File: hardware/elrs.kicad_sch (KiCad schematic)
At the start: 38 parts, among them J10 5V, J11 5V, J12 5V, J26 5V, J31 5V, U12 WL9005D4-33, U19 XL-1010RGBC-WS2812B, U2 ESP32-C3FH4, U20 SX1281IMLTRT, X2 SX0B40.000F0810F30

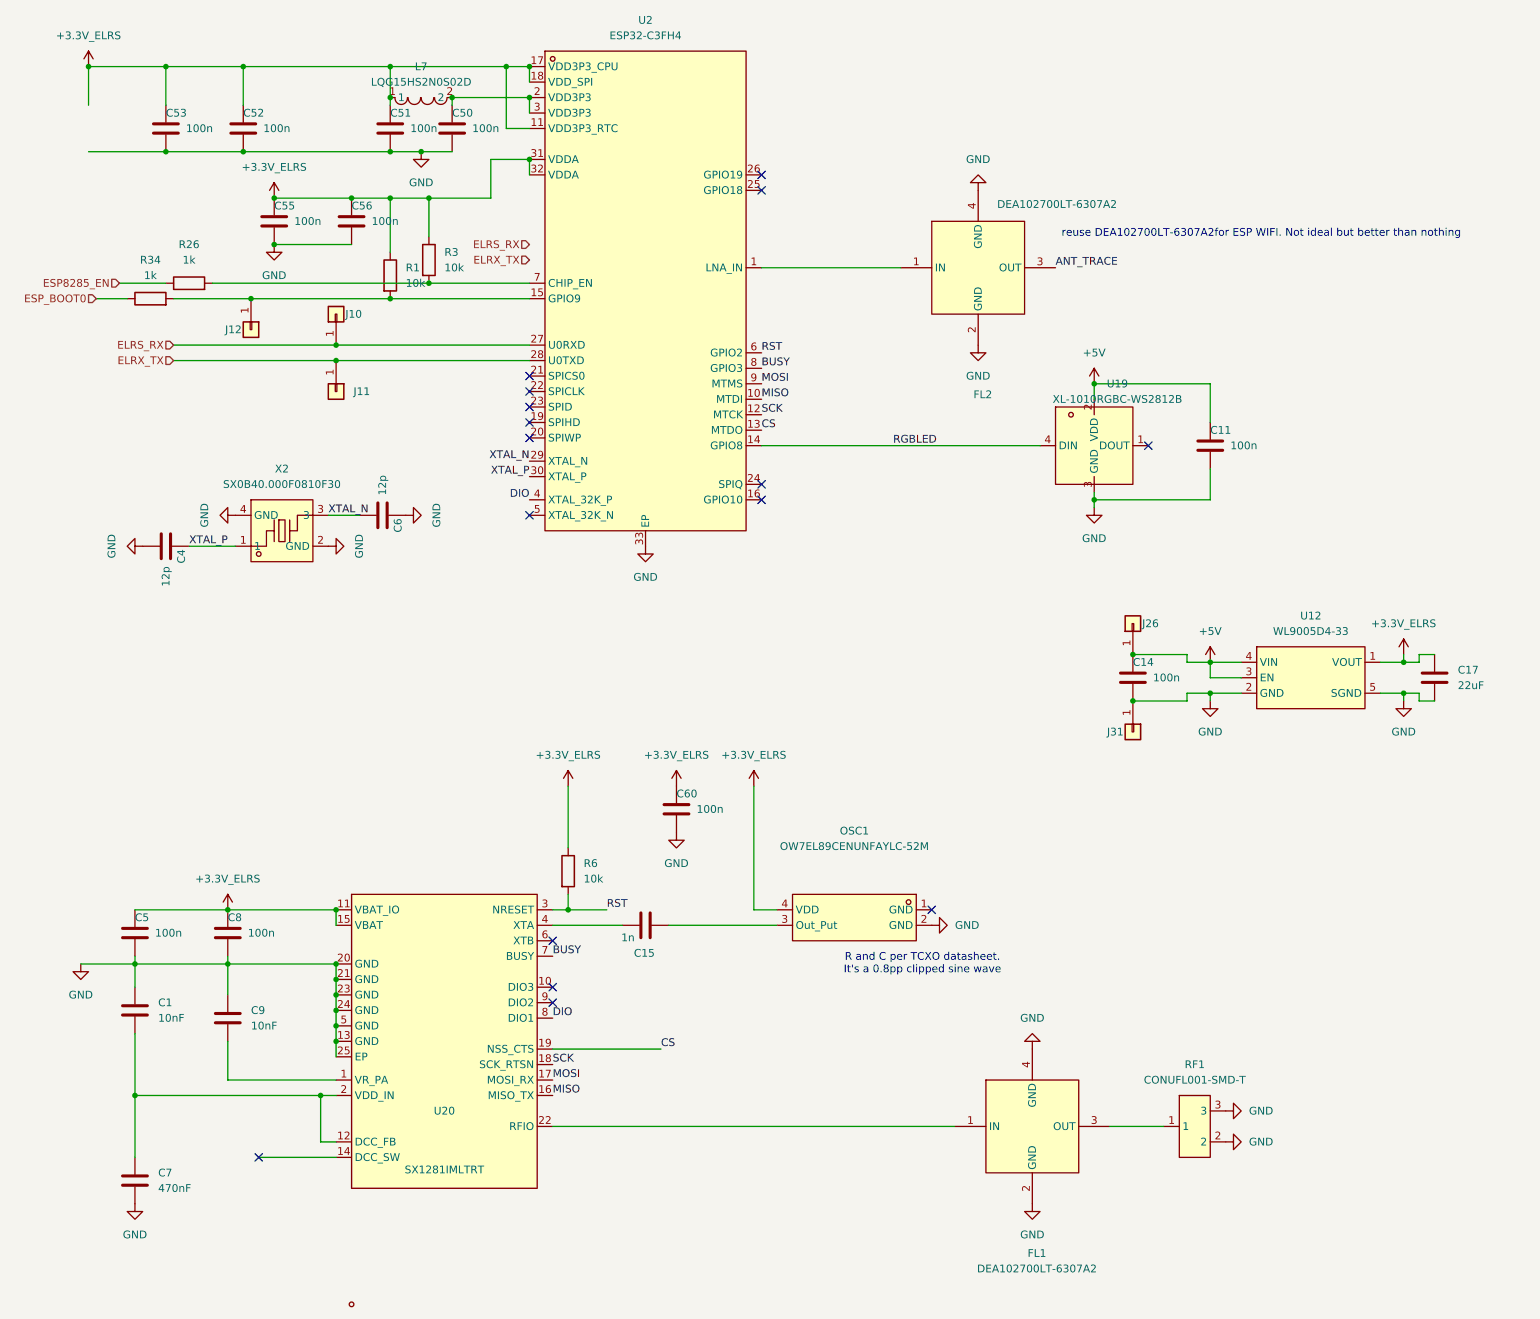
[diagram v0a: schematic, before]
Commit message: switched to 0201
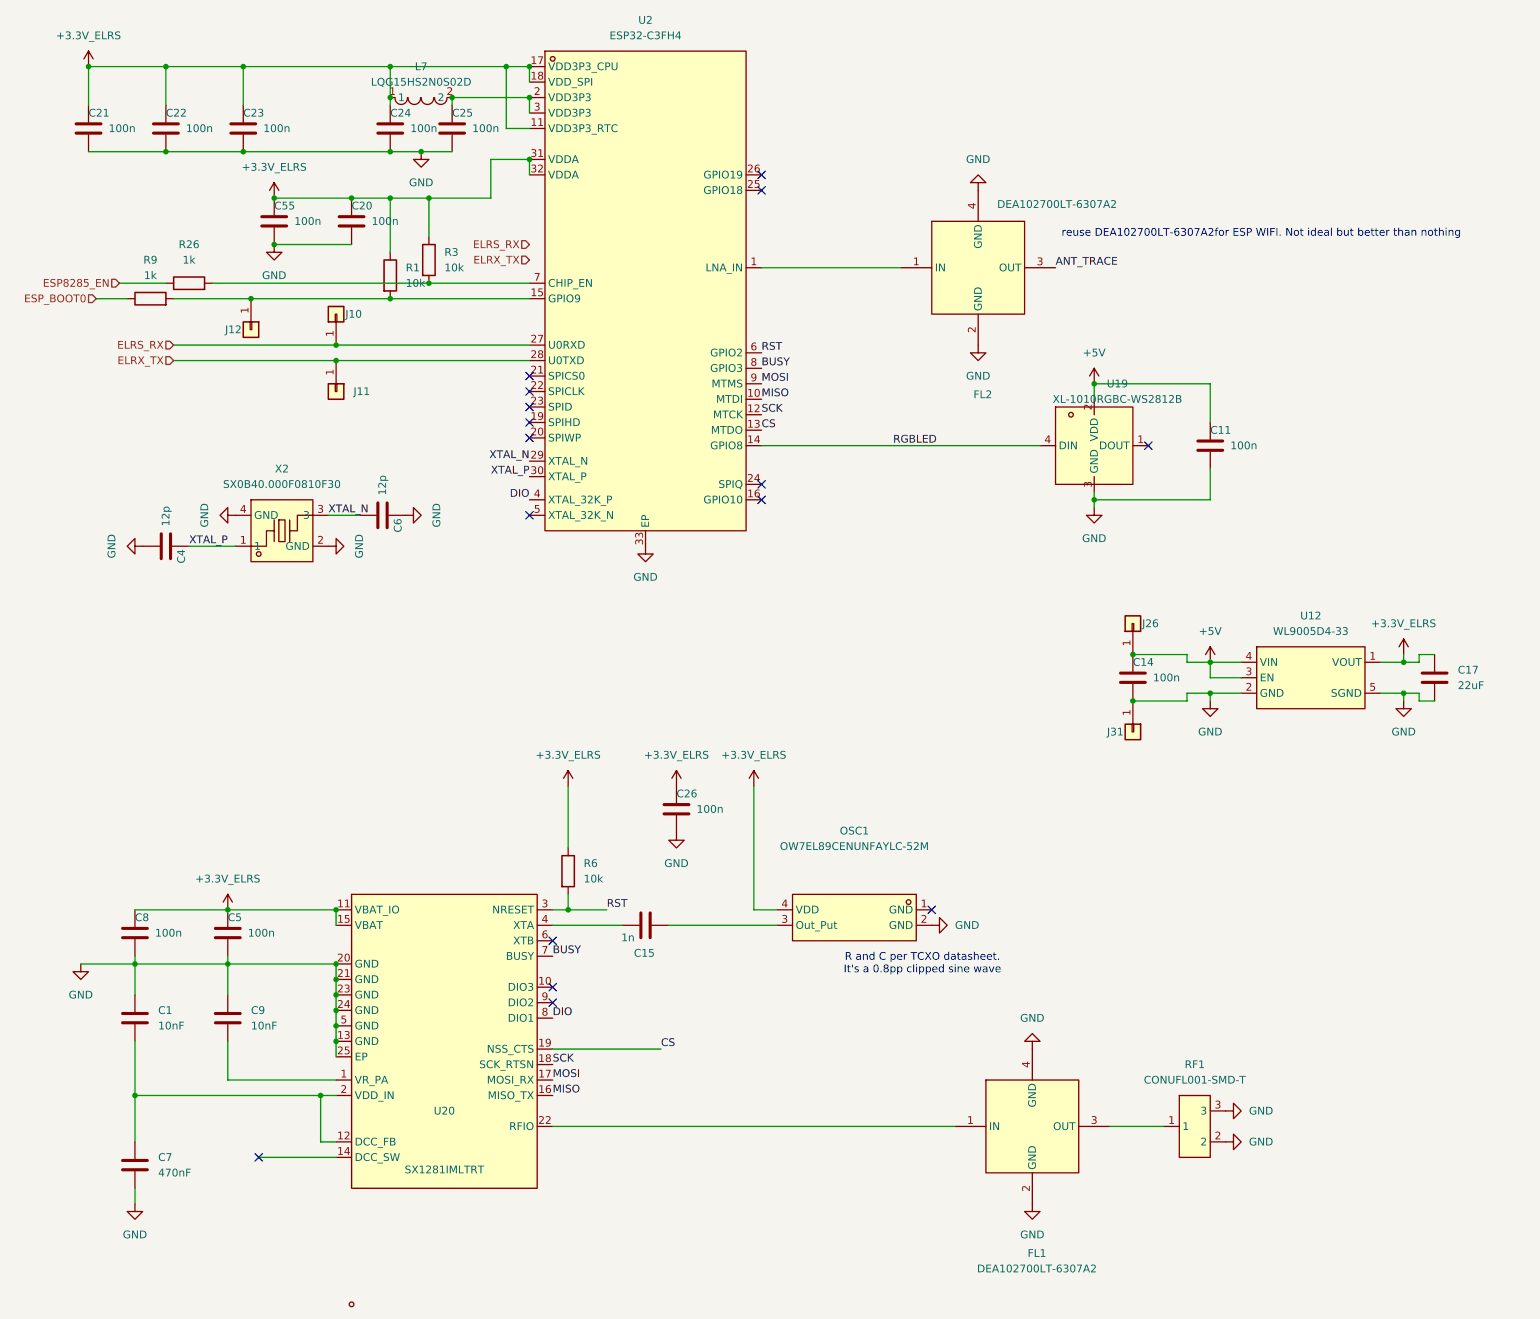
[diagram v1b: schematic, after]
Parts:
- removed C50, C51, C52, C53, C56, C60: 100n, Capacitor_SMD:C_0402_1005Metric, symbol Device:C
- removed R34: 1k, Resistor_SMD:R_0402_1005Metric, symbol Device:R
- added C20, C21, C22, C23, C24, C25, C26: 100n, Capacitor_SMD:C_0201_0603Metric, symbol Device:C
- added R9: 1k, Capacitor_SMD:C_0201_0603Metric, symbol Device:R
- C1, C9: footprint Capacitor_SMD:C_0402_1005Metric -> Capacitor_SMD:C_0201_0603Metric; LCSC C15195 -> C76941
- C11, C14, C5, C55, C8: footprint Capacitor_SMD:C_0402_1005Metric -> Capacitor_SMD:C_0201_0603Metric; LCSC C1525 -> C76939
- C15: footprint Capacitor_SMD:C_0402_1005Metric -> Capacitor_SMD:C_0201_0603Metric; LCSC (none) -> C85934
- C4, C6: footprint Capacitor_SMD:C_0402_1005Metric -> Capacitor_SMD:C_0201_0603Metric; LCSC C441742 -> C161404
- C7: footprint Capacitor_SMD:C_0402_1005Metric -> Capacitor_SMD:C_0201_0603Metric; LCSC C92361 -> C85926
- R1, R3, R6: footprint Resistor_SMD:R_0402_1005Metric -> Capacitor_SMD:C_0201_0603Metric; LCSC C2909316 -> C473048
- R26: footprint Resistor_SMD:R_0402_1005Metric -> Capacitor_SMD:C_0201_0603Metric; LCSC C2909316 -> C270365
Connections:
- net +3.3V_ELRS: now also C20.1, C21.1, C22.1, C23.1, C24.1, C26.1
- net ESP_BOOT0: now also R9.1
- net GND: now also C20.2, C21.2, C22.2, C23.2, C24.2, C25.2, C26.2
- net at J12.1 (Pin_1), R1.2, U2.15 (GPIO9): now also R9.2
- net at L7.2, U2.2 (VDD3P3), U2.3 (VDD3P3): now also C25.1
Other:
- moved on the sheet: C1, C7
